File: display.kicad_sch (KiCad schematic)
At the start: 32 parts, among them Q1 AO3401A, Q2 BSS138

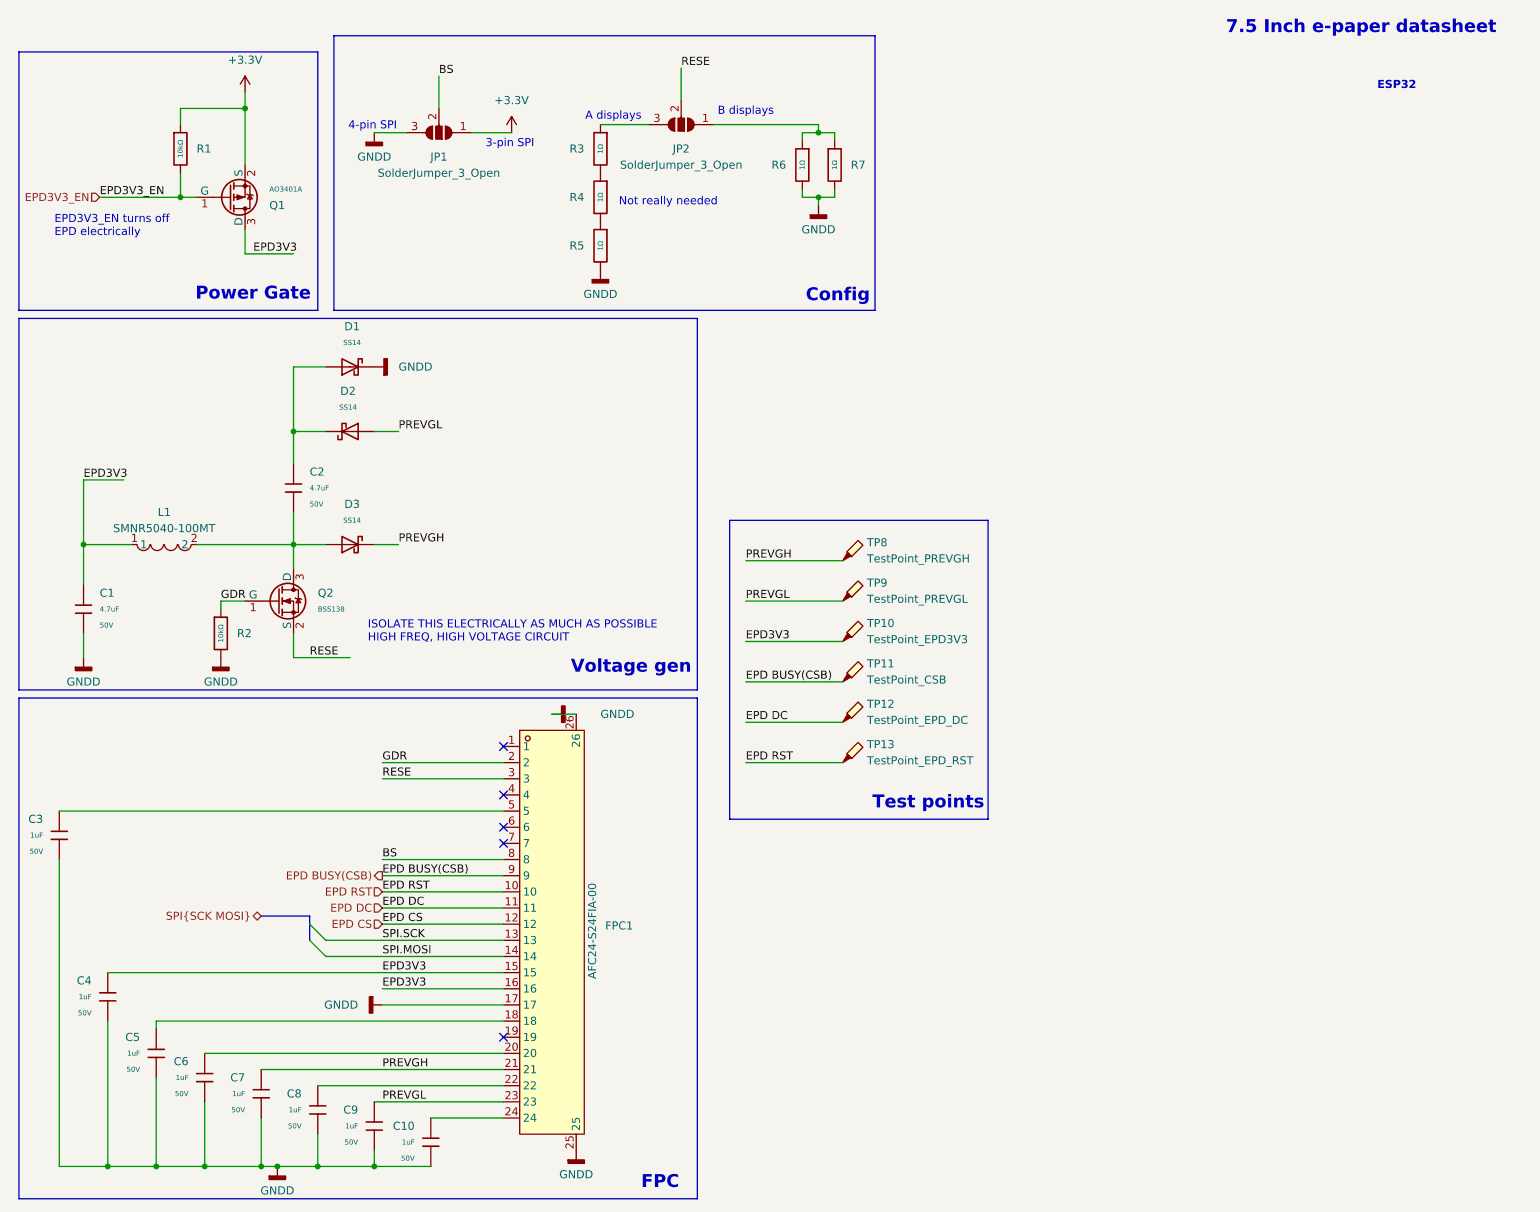
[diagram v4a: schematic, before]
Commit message: Schematic cleanup and initial layout complete
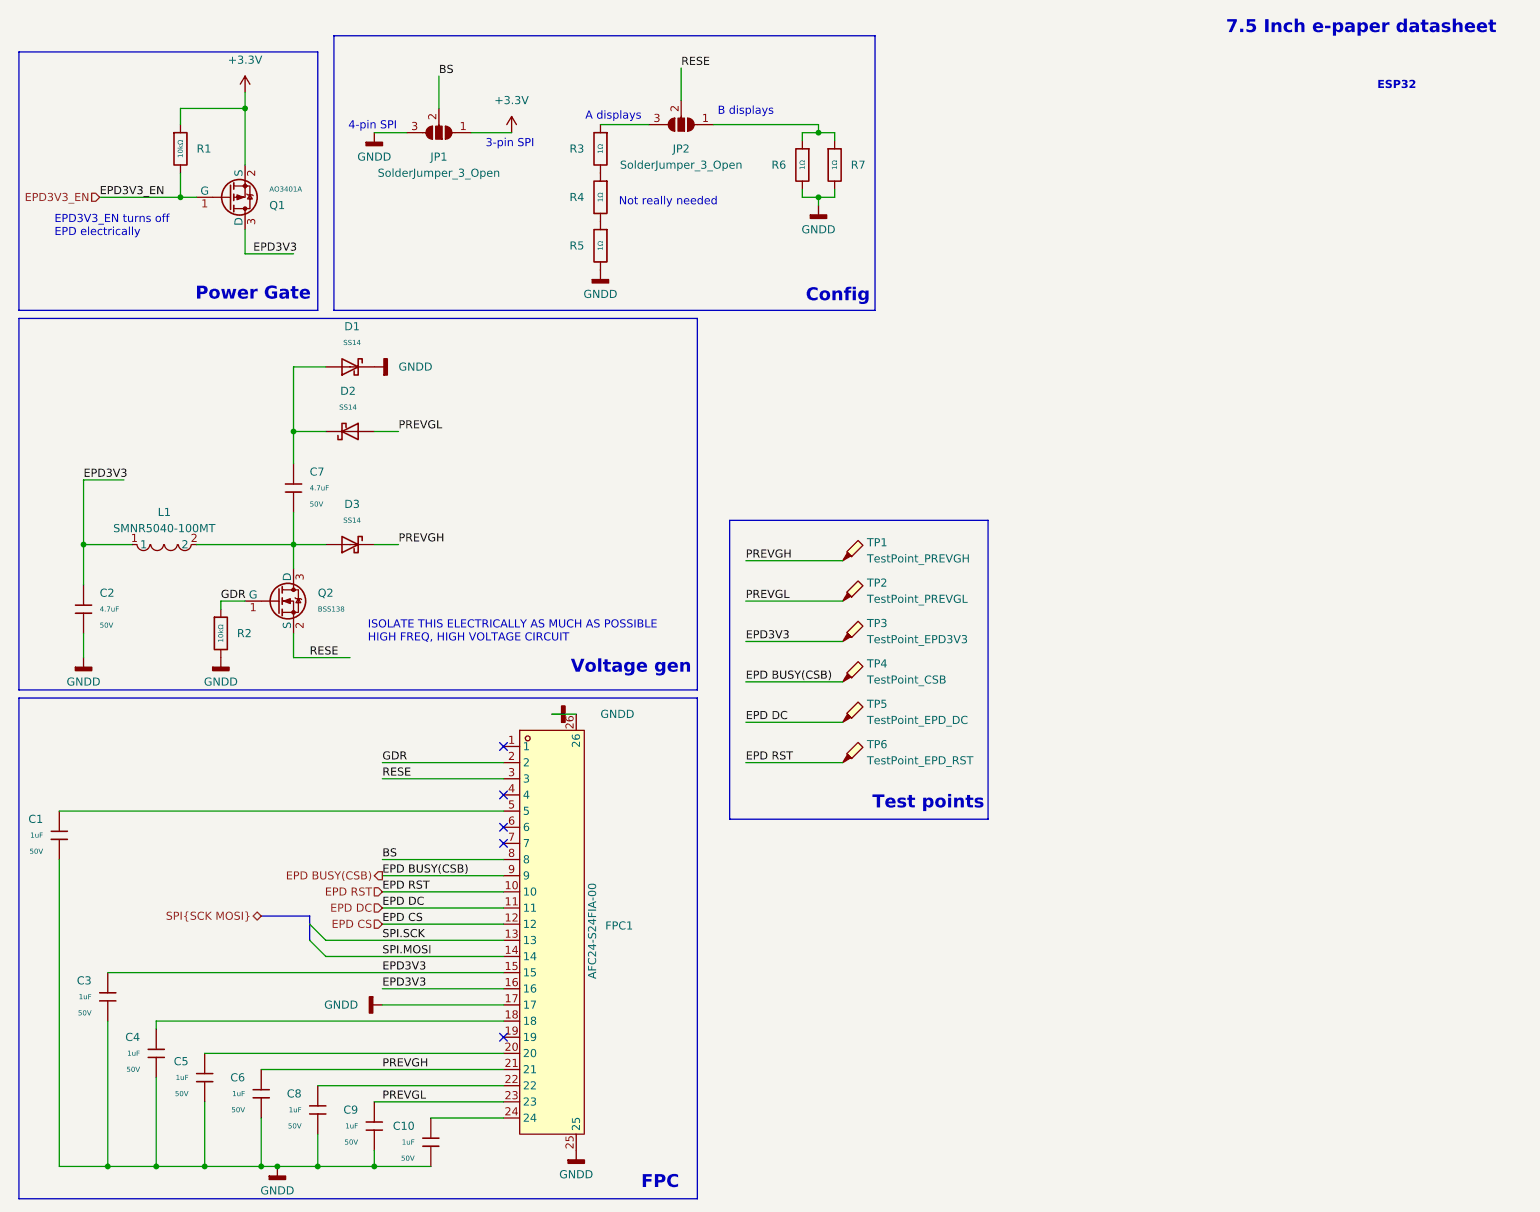
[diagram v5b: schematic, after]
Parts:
- renumbered C3 to C1, C1 to C2, C4 to C3, C5 to C4, C6 to C5, C7 to C6, C2 to C7, TP8 to TP1, TP9 to TP2, TP10 to TP3, TP11 to TP4, TP12 to TP5, TP13 to TP6
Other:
- company: (none) -> Josef
- title: (none) -> EPD
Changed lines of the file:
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@@
 	(generator_version "9.0")
 	(paper "A4")
+	(title_block
+		(title "EPD")
+		(date "2026-03-19")
+		(rev "1.0")
+		(company "Josef")
+	)
 	(rectangle
 		(start 129.54 91.44)
@@
 		(dnp no)
 		(fields_autoplaced yes)
-		(property "Reference" "TP8"
+		(property "Reference" "TP1"
 			(at 151.13 94.9324 0)
 			(effects
@@
 			(project "E-paper-picture-frame-HW"
 				(path "/84f37c25-92ec-4cd3-b0ad-d93e10e73cdb/9b514820-994d-4acc-ba3e-efc41ebe2f4e"
-					(reference "TP8")
+					(reference "TP1")
 					(unit 1)
 				)
@@
 		(dnp no)
 		(fields_autoplaced yes)
-		(property "Reference" "C6"
+		(property "Reference" "C5"
 			(at 44.45 176.5299 0)
 			(effects
@@
 			(project "E-paper-picture-frame-HW"
 				(path "/84f37c25-92ec-4cd3-b0ad-d93e10e73cdb/9b514820-994d-4acc-ba3e-efc41ebe2f4e"
-					(reference "C6")
+					(reference "C5")
 					(unit 1)
 				)
@@
 		(dnp no)
 		(fields_autoplaced yes)
-		(property "Reference" "C3"
+		(property "Reference" "C1"
 			(at 21.59 138.4299 0)
 			(effects
@@
 			(project ""
 				(path "/84f37c25-92ec-4cd3-b0ad-d93e10e73cdb/9b514820-994d-4acc-ba3e-efc41ebe2f4e"
-					(reference "C3")
+					(reference "C1")
 					(unit 1)
 				)
@@
 		(dnp no)
 		(fields_autoplaced yes)
-		(property "Reference" "C2"
+		(property "Reference" "C7"
 			(at 63.5 83.8199 0)
 			(effects
@@
 			(project "E-paper-picture-frame-HW"
 				(path "/84f37c25-92ec-4cd3-b0ad-d93e10e73cdb/9b514820-994d-4acc-ba3e-efc41ebe2f4e"
-					(reference "C2")
+					(reference "C7")
 					(unit 1)
 				)
@@
 		(dnp no)
 		(fields_autoplaced yes)
-		(property "Reference" "TP11"
+		(property "Reference" "TP4"
 			(at 151.13 113.9824 0)
 			(effects
@@
 			(project "E-paper-picture-frame-HW"
 				(path "/84f37c25-92ec-4cd3-b0ad-d93e10e73cdb/9b514820-994d-4acc-ba3e-efc41ebe2f4e"
-					(reference "TP11")
+					(reference "TP4")
 					(unit 1)
 				)
@@
 		(dnp no)
 		(fields_autoplaced yes)
-		(property "Reference" "#PWR06"
+		(property "Reference" "#PWR08"
 			(at 95.25 34.29 0)
 			(effects
@@
 			(project ""
 				(path "/84f37c25-92ec-4cd3-b0ad-d93e10e73cdb/9b514820-994d-4acc-ba3e-efc41ebe2f4e"
-					(reference "#PWR06")
+					(reference "#PWR08")
 					(unit 1)
 				)
@@
 		(dnp no)
 		(fields_autoplaced yes)
-		(property "Reference" "#PWR05"
+		(property "Reference" "#PWR06"
 			(at 80.01 67.31 0)
 			(effects
@@
 			(project "E-paper-picture-frame-HW"
 				(path "/84f37c25-92ec-4cd3-b0ad-d93e10e73cdb/9b514820-994d-4acc-ba3e-efc41ebe2f4e"
-					(reference "#PWR05")
+					(reference "#PWR06")
 					(unit 1)
 				)
@@
 		(dnp no)
 		(fields_autoplaced yes)
-		(property "Reference" "#PWR08"
+		(property "Reference" "#PWR011"
 			(at 109.22 58.42 0)
 			(effects
@@
 			(project "E-paper-picture-frame-HW"
 				(path "/84f37c25-92ec-4cd3-b0ad-d93e10e73cdb/9b514820-994d-4acc-ba3e-efc41ebe2f4e"
-					(reference "#PWR08")
+					(reference "#PWR011")
 					(unit 1)
 				)
@@
 		(dnp no)
 		(fields_autoplaced yes)
-		(property "Reference" "#PWR07"
+		(property "Reference" "#PWR04"
 			(at 58.42 199.39 0)
 			(effects
@@
 			(project "E-paper-picture-frame-HW"
 				(path "/84f37c25-92ec-4cd3-b0ad-d93e10e73cdb/9b514820-994d-4acc-ba3e-efc41ebe2f4e"
-					(reference "#PWR07")
+					(reference "#PWR04")
 					(unit 1)
 				)
@@
 		(dnp no)
 		(fields_autoplaced yes)
-		(property "Reference" "TP12"
+		(property "Reference" "TP5"
 			(at 151.13 120.3324 0)
 			(effects
@@
 			(project "E-paper-picture-frame-HW"
 				(path "/84f37c25-92ec-4cd3-b0ad-d93e10e73cdb/9b514820-994d-4acc-ba3e-efc41ebe2f4e"
-					(reference "TP12")
+					(reference "TP5")
 					(unit 1)
 				)
@@
 		(dnp no)
 		(fields_autoplaced yes)
-		(property "Reference" "C1"
+		(property "Reference" "C2"
 			(at 30.48 102.8699 0)
 			(effects
@@
 			(project ""
 				(path "/84f37c25-92ec-4cd3-b0ad-d93e10e73cdb/9b514820-994d-4acc-ba3e-efc41ebe2f4e"
-					(reference "C1")
+					(reference "C2")
 					(unit 1)
 				)
@@
 		(dnp no)
 		(fields_autoplaced yes)
-		(property "Reference" "C5"
+		(property "Reference" "C4"
 			(at 36.83 172.7199 0)
 			(effects
@@
 			(project "E-paper-picture-frame-HW"
 				(path "/84f37c25-92ec-4cd3-b0ad-d93e10e73cdb/9b514820-994d-4acc-ba3e-efc41ebe2f4e"
-					(reference "C5")
+					(reference "C4")
 					(unit 1)
 				)
@@
 		(on_board yes)
 		(dnp no)
-		(property "Reference" "#PWR011"
+		(property "Reference" "#PWR09"
 			(at 107.95 121.92 0)
 			(effects
@@
 			(project "E-paper-picture-frame-HW"
 				(path "/84f37c25-92ec-4cd3-b0ad-d93e10e73cdb/9b514820-994d-4acc-ba3e-efc41ebe2f4e"
-					(reference "#PWR011")
+					(reference "#PWR09")
 					(unit 1)
 				)
@@
 		(dnp no)
 		(fields_autoplaced yes)
-		(property "Reference" "TP9"
+		(property "Reference" "TP2"
 			(at 151.13 101.2824 0)
 			(effects
@@
 			(project "E-paper-picture-frame-HW"
 				(path "/84f37c25-92ec-4cd3-b0ad-d93e10e73cdb/9b514820-994d-4acc-ba3e-efc41ebe2f4e"
-					(reference "TP9")
+					(reference "TP2")
 					(unit 1)
 				)
@@
 		(dnp no)
 		(fields_autoplaced yes)
-		(property "Reference" "C4"
+		(property "Reference" "C3"
 			(at 29.21 163.8299 0)
 			(effects
@@
 			(project "E-paper-picture-frame-HW"
 				(path "/84f37c25-92ec-4cd3-b0ad-d93e10e73cdb/9b514820-994d-4acc-ba3e-efc41ebe2f4e"
-					(reference "C4")
+					(reference "C3")
 					(unit 1)
 				)
@@
 		(dnp no)
 		(fields_autoplaced yes)
-		(property "Reference" "#PWR010"
+		(property "Reference" "#PWR012"
 			(at 143.51 48.26 0)
 			(effects
@@
 			(project "E-paper-picture-frame-HW"
 				(path "/84f37c25-92ec-4cd3-b0ad-d93e10e73cdb/9b514820-994d-4acc-ba3e-efc41ebe2f4e"
-					(reference "#PWR010")
+					(reference "#PWR012")
 					(unit 1)
 				)
@@
 		(dnp no)
 		(fields_autoplaced yes)
-		(property "Reference" "TP13"
+		(property "Reference" "TP6"
 			(at 151.13 126.6824 0)
 			(effects
@@
 			(project "E-paper-picture-frame-HW"
 				(path "/84f37c25-92ec-4cd3-b0ad-d93e10e73cdb/9b514820-994d-4acc-ba3e-efc41ebe2f4e"
-					(reference "TP13")
+					(reference "TP6")
 					(unit 1)
 				)
@@
 		(dnp no)
 		(fields_autoplaced yes)
-		(property "Reference" "TP10"
+		(property "Reference" "TP3"
 			(at 151.13 107.6324 0)
 			(effects
@@
 			(project "E-paper-picture-frame-HW"
 				(path "/84f37c25-92ec-4cd3-b0ad-d93e10e73cdb/9b514820-994d-4acc-ba3e-efc41ebe2f4e"
-					(reference "TP10")
+					(reference "TP3")
 					(unit 1)
 				)
@@
 		(dnp no)
 		(fields_autoplaced yes)
-		(property "Reference" "#PWR09"
+		(property "Reference" "#PWR07"
 			(at 68.58 167.64 0)
 			(effects
@@
 			(project "E-paper-picture-frame-HW"
 				(path "/84f37c25-92ec-4cd3-b0ad-d93e10e73cdb/9b514820-994d-4acc-ba3e-efc41ebe2f4e"
-					(reference "#PWR09")
+					(reference "#PWR07")
 					(unit 1)
 				)
@@
 		(dnp no)
 		(fields_autoplaced yes)
-		(property "Reference" "#PWR012"
+		(property "Reference" "#PWR010"
 			(at 105.41 196.85 0)
 			(effects
@@
 			(project "E-paper-picture-frame-HW"
 				(path "/84f37c25-92ec-4cd3-b0ad-d93e10e73cdb/9b514820-994d-4acc-ba3e-efc41ebe2f4e"
-					(reference "#PWR012")
+					(reference "#PWR010")
 					(unit 1)
 				)
@@
 		(dnp no)
 		(fields_autoplaced yes)
-		(property "Reference" "C7"
+		(property "Reference" "C6"
 			(at 53.34 179.0699 0)
 			(effects
@@
 			(project "E-paper-picture-frame-HW"
 				(path "/84f37c25-92ec-4cd3-b0ad-d93e10e73cdb/9b514820-994d-4acc-ba3e-efc41ebe2f4e"
-					(reference "C7")
+					(reference "C6")
 					(unit 1)
 				)
@@
 		(dnp no)
 		(fields_autoplaced yes)
-		(property "Reference" "#PWR04"
+		(property "Reference" "#PWR05"
 			(at 73.66 36.83 0)
 			(effects
@@
 			(project ""
 				(path "/84f37c25-92ec-4cd3-b0ad-d93e10e73cdb/9b514820-994d-4acc-ba3e-efc41ebe2f4e"
-					(reference "#PWR04")
+					(reference "#PWR05")
 					(unit 1)
 				)

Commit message: Small cleanup + linked jlcpcb parts for ordering
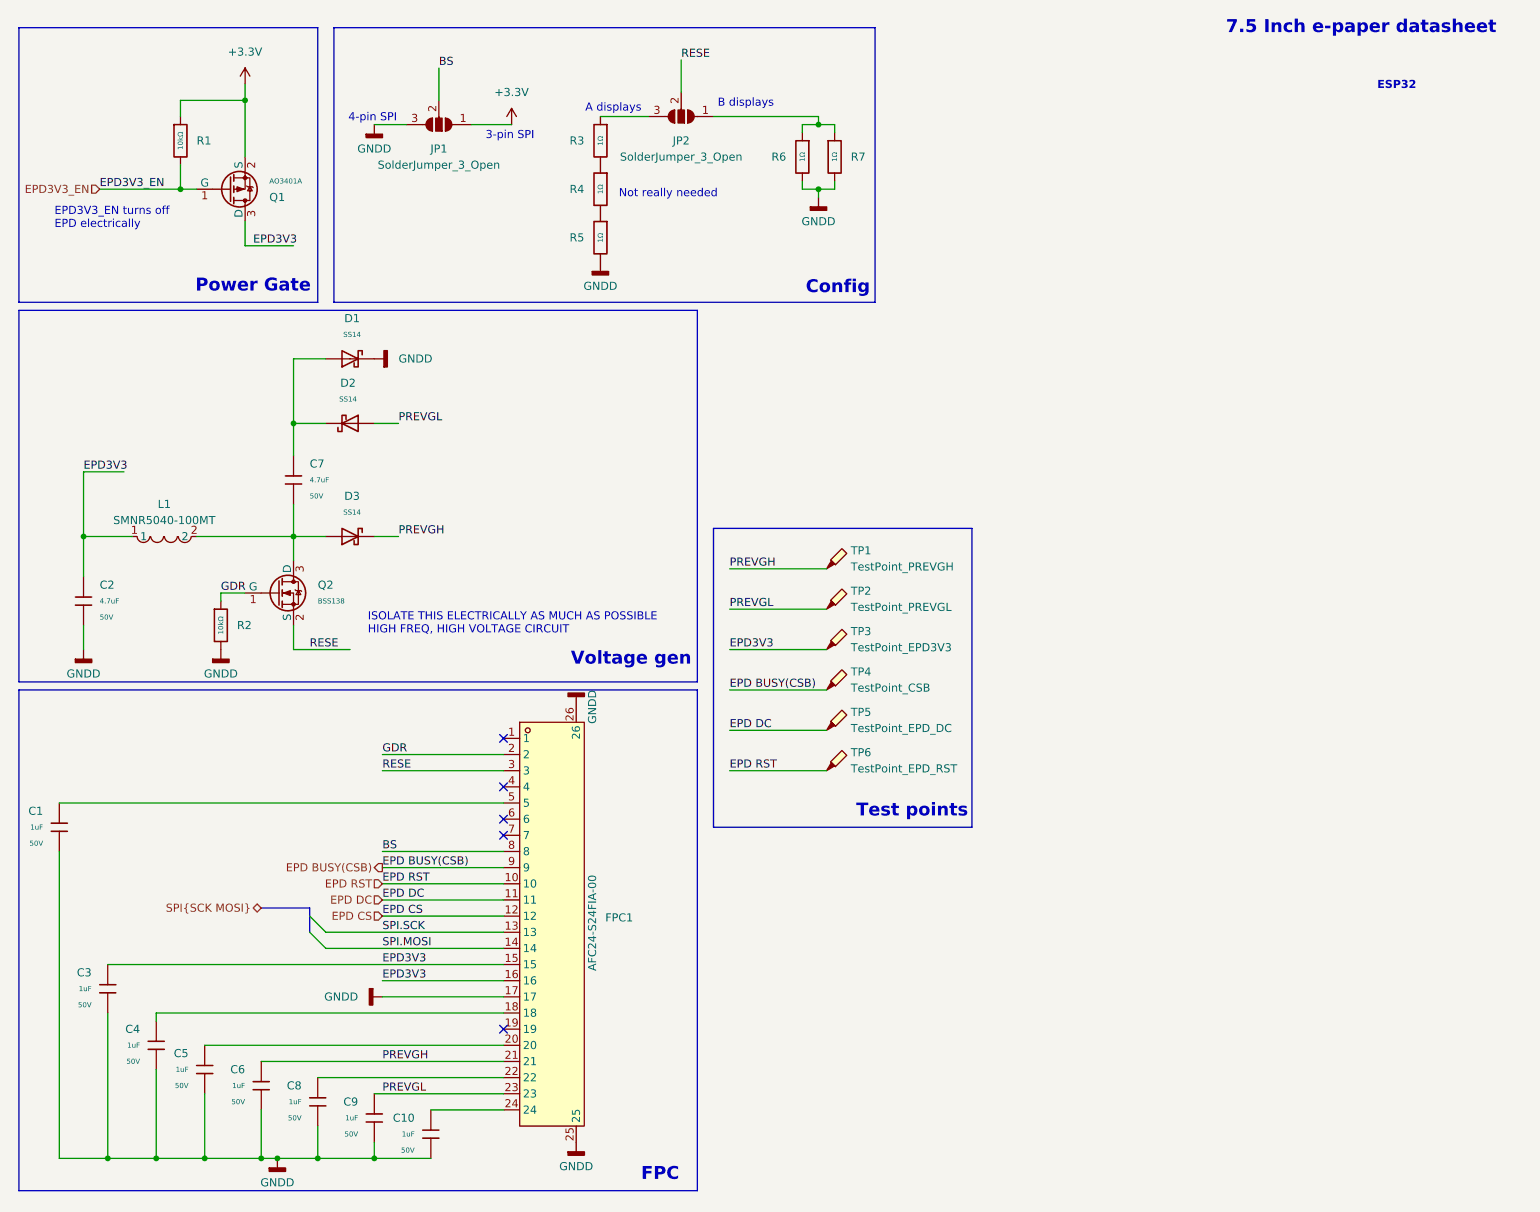
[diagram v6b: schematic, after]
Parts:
- L1: footprint shielded_ind:IND-SMD_2P-L5.0-W5.0 -> Libraries:IND-SMD_2P-L5.0-W5.0
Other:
- moved on the sheet: C1, C10, C2, C3, C4, C5, C6, C7, C8, C9, D1, D2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
